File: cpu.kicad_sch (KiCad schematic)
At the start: 22 parts, among them IC1 68HC000

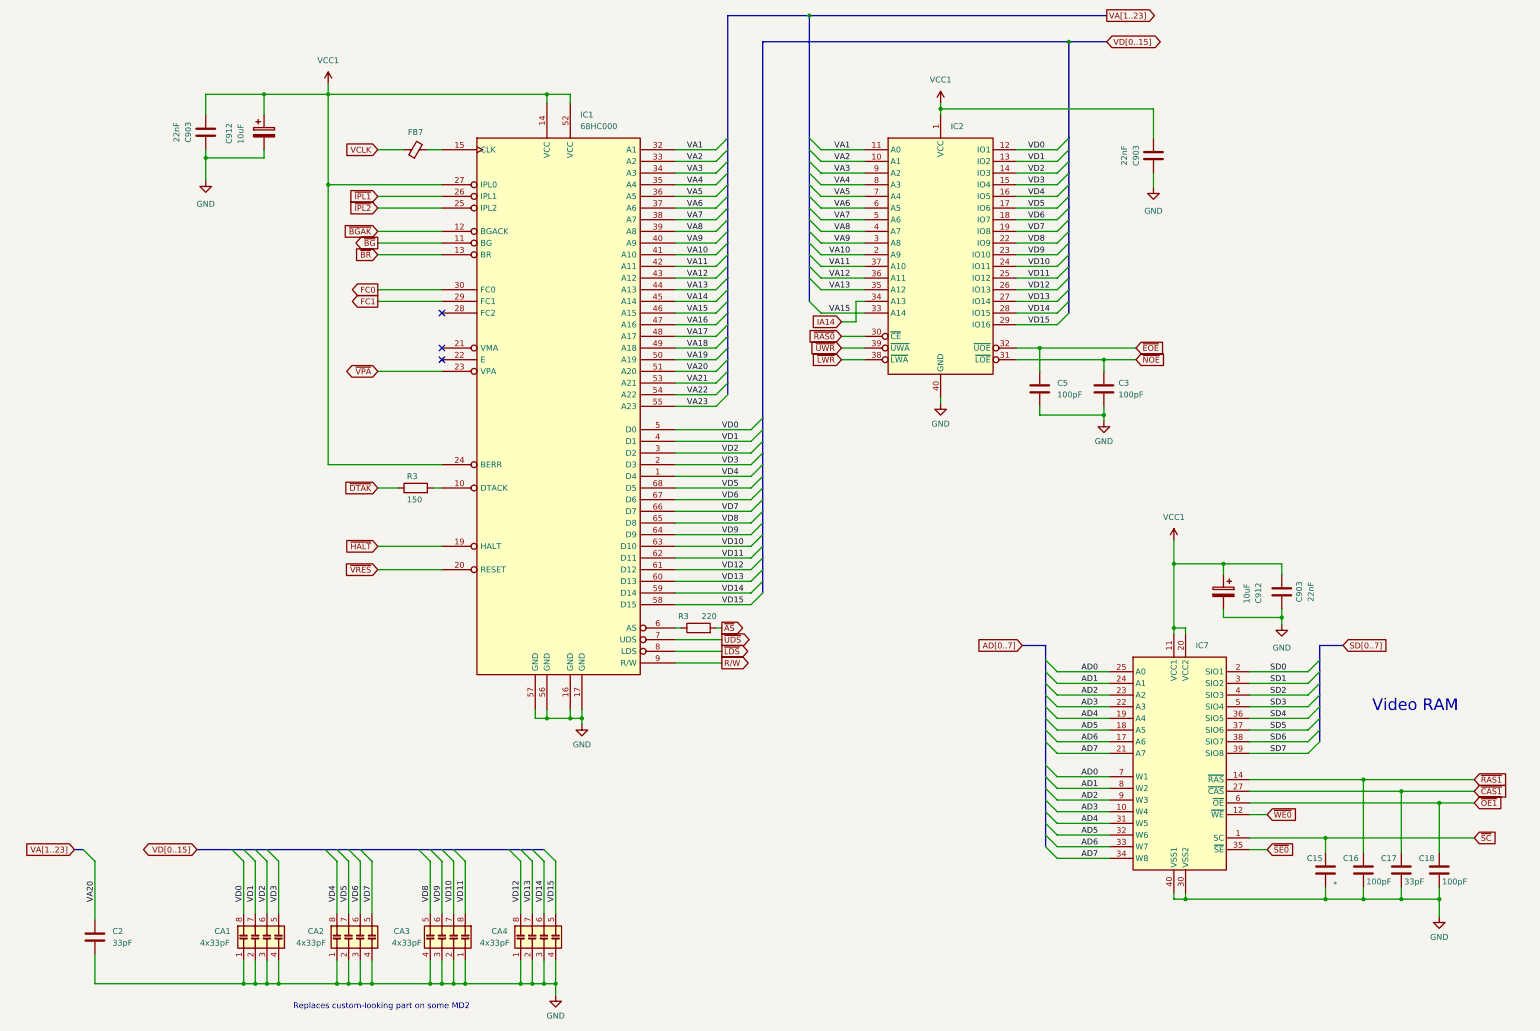
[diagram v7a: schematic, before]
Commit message: Review/add 32X bodges.
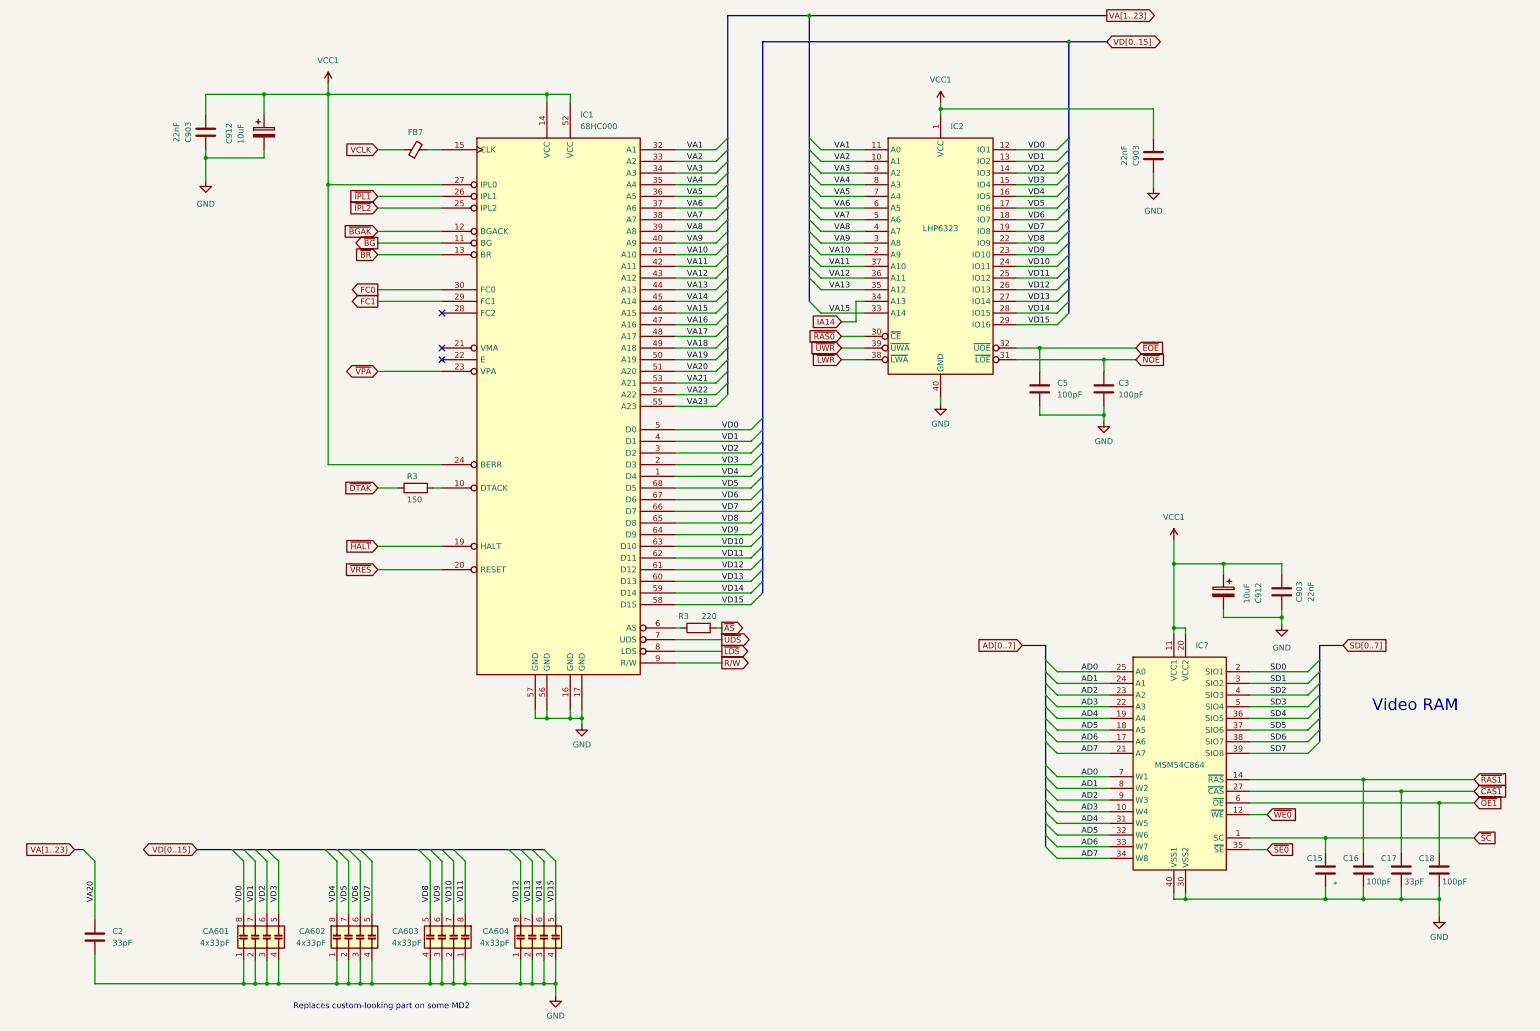
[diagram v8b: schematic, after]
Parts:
- IC2: value ~ -> LHP6323
- IC7: value ~ -> MSM54C864
- renumbered CA1 to CA601, CA2 to CA602, CA3 to CA603, CA4 to CA604
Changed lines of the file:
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@@
   (symbol (lib_id "MegaDrive:C_Pack04") (at 140.97 231.14 0) (mirror y) (unit 1)
     (in_bom yes) (on_board yes) (dnp no)
-    (property "Reference" "CA3" (at 133.985 229.87 0)
+    (property "Reference" "CA603" (at 135.89 229.87 0)
       (effects (font (size 1.27 1.27)) (justify left))
     )
@@
       (project "Neptune"
         (path "/bcc23b51-b742-4ae5-9dd6-d96a24058944/48e60f61-77cc-4ea0-898f-0029aa970ca5"
-          (reference "CA3") (unit 1)
+          (reference "CA603") (unit 1)
         )
       )
@@
   )
   (symbol (lib_id "MegaDrive:VRAM_64Kx8") (at 301.625 193.675 0) (unit 1)
-    (in_bom yes) (on_board yes) (dnp no) (fields_autoplaced)
+    (in_bom yes) (on_board yes) (dnp no)
     (property "Reference" "IC7" (at 305.0891 167.64 0)
       (effects (font (size 1.27 1.27)) (justify left))
     )
-    (property "Value" "~" (at 302.26 196.85 0)
+    (property "Value" "MSM54C864" (at 301.625 193.675 0)
       (effects (font (size 1.27 1.27)))
     )
@@
   (symbol (lib_id "MegaDrive:C_Pack04") (at 102.87 231.14 0) (unit 1)
     (in_bom yes) (on_board yes) (dnp no)
-    (property "Reference" "CA1" (at 91.44 229.87 0)
+    (property "Reference" "CA601" (at 88.9 229.87 0)
       (effects (font (size 1.27 1.27)) (justify left))
     )
@@
       (project "Neptune"
         (path "/bcc23b51-b742-4ae5-9dd6-d96a24058944/48e60f61-77cc-4ea0-898f-0029aa970ca5"
-          (reference "CA1") (unit 1)
+          (reference "CA601") (unit 1)
         )
       )
@@
   (symbol (lib_id "MegaDrive:C_Pack04") (at 123.19 231.14 0) (unit 1)
     (in_bom yes) (on_board yes) (dnp no)
-    (property "Reference" "CA2" (at 111.76 229.87 0)
+    (property "Reference" "CA602" (at 109.855 229.87 0)
       (effects (font (size 1.27 1.27)) (justify left))
     )
@@
       (project "Neptune"
         (path "/bcc23b51-b742-4ae5-9dd6-d96a24058944/48e60f61-77cc-4ea0-898f-0029aa970ca5"
-          (reference "CA2") (unit 1)
+          (reference "CA602") (unit 1)
         )
       )
@@
   (symbol (lib_id "MegaDrive:C_Pack04") (at 163.195 231.14 0) (unit 1)
     (in_bom yes) (on_board yes) (dnp no)
-    (property "Reference" "CA4" (at 151.765 229.87 0)
+    (property "Reference" "CA604" (at 149.86 229.87 0)
       (effects (font (size 1.27 1.27)) (justify left))
     )
@@
       (project "Neptune"
         (path "/bcc23b51-b742-4ae5-9dd6-d96a24058944/48e60f61-77cc-4ea0-898f-0029aa970ca5"
-          (reference "CA4") (unit 1)
+          (reference "CA604") (unit 1)
         )
       )
@@
       (effects (font (size 1.27 1.27)) (justify left))
     )
-    (property "Value" "~" (at 249.555 76.835 0)
-      (effects (font (size 1.27 1.27)))
-    )
+    (property "Value" "LHP6323" (at 249.555 76.835 0)
+      (effects (font (size 1.27 1.27)))
+    )
